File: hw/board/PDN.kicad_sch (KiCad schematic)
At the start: 47 parts, among them U1 XC7A35T-FTG256, U2 TPS54331DR, U3 AP7361C-18SP-13, U4 AP7361C-10E

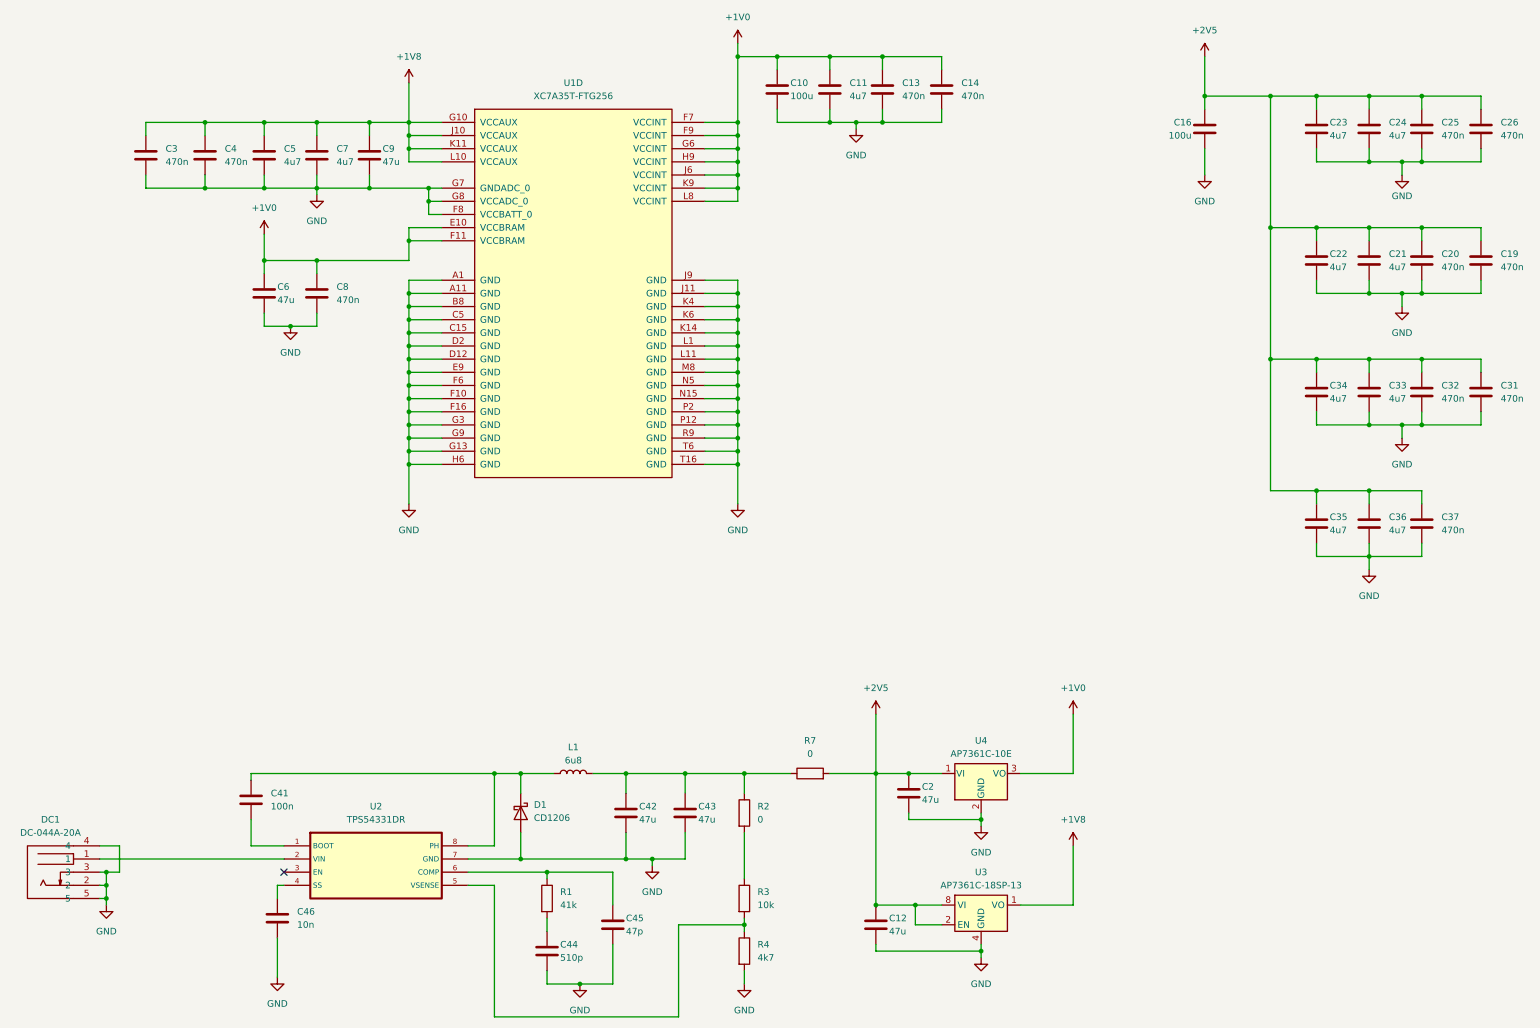
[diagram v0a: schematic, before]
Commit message: Reannotated piece numbers
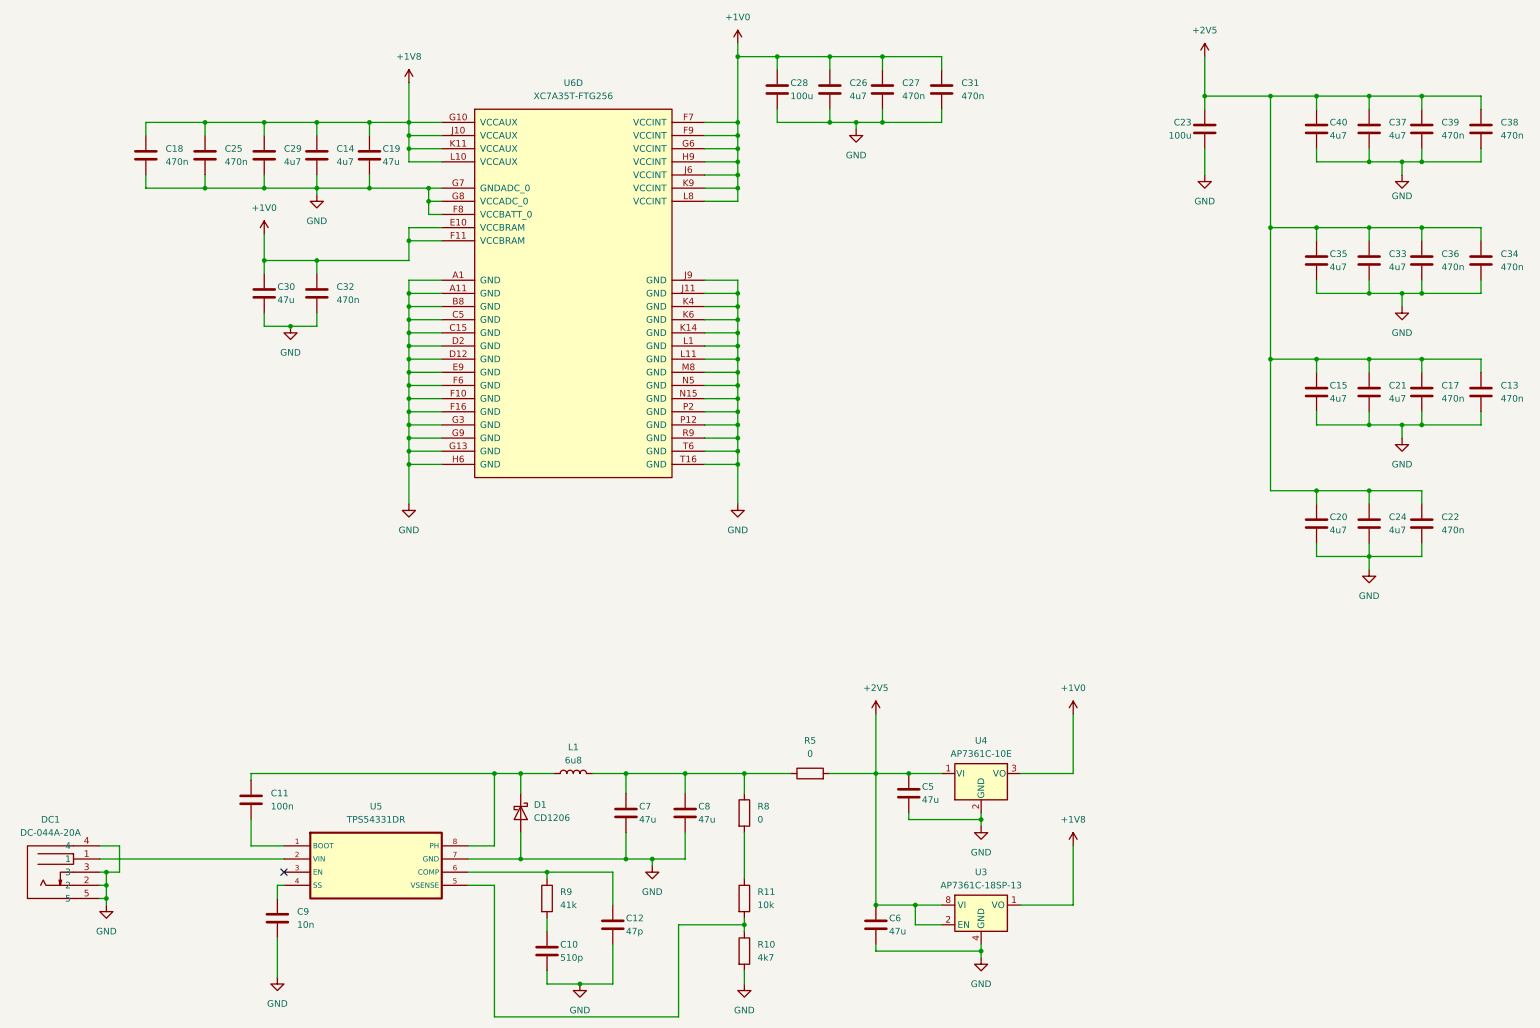
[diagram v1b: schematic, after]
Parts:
- renumbered C44 to C10, C41 to C11, C45 to C12, C31 to C13, C7 to C14, C34 to C15, C32 to C17, C3 to C18, C9 to C19, C35 to C20, C33 to C21, C37 to C22, C16 to C23, C36 to C24, C4 to C25, C11 to C26, C13 to C27, C10 to C28, C5 to C29, C6 to C30, C14 to C31, C8 to C32, C21 to C33, C19 to C34, C22 to C35, C20 to C36, C24 to C37, C26 to C38, C25 to C39, C23 to C40, C2 to C5, C12 to C6, C42 to C7, C43 to C8, C46 to C9, R4 to R10, R3 to R11, R7 to R5, R2 to R8, R1 to R9, U2 to U5, U1 to U6

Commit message: Added capacitor for STM32 NRST
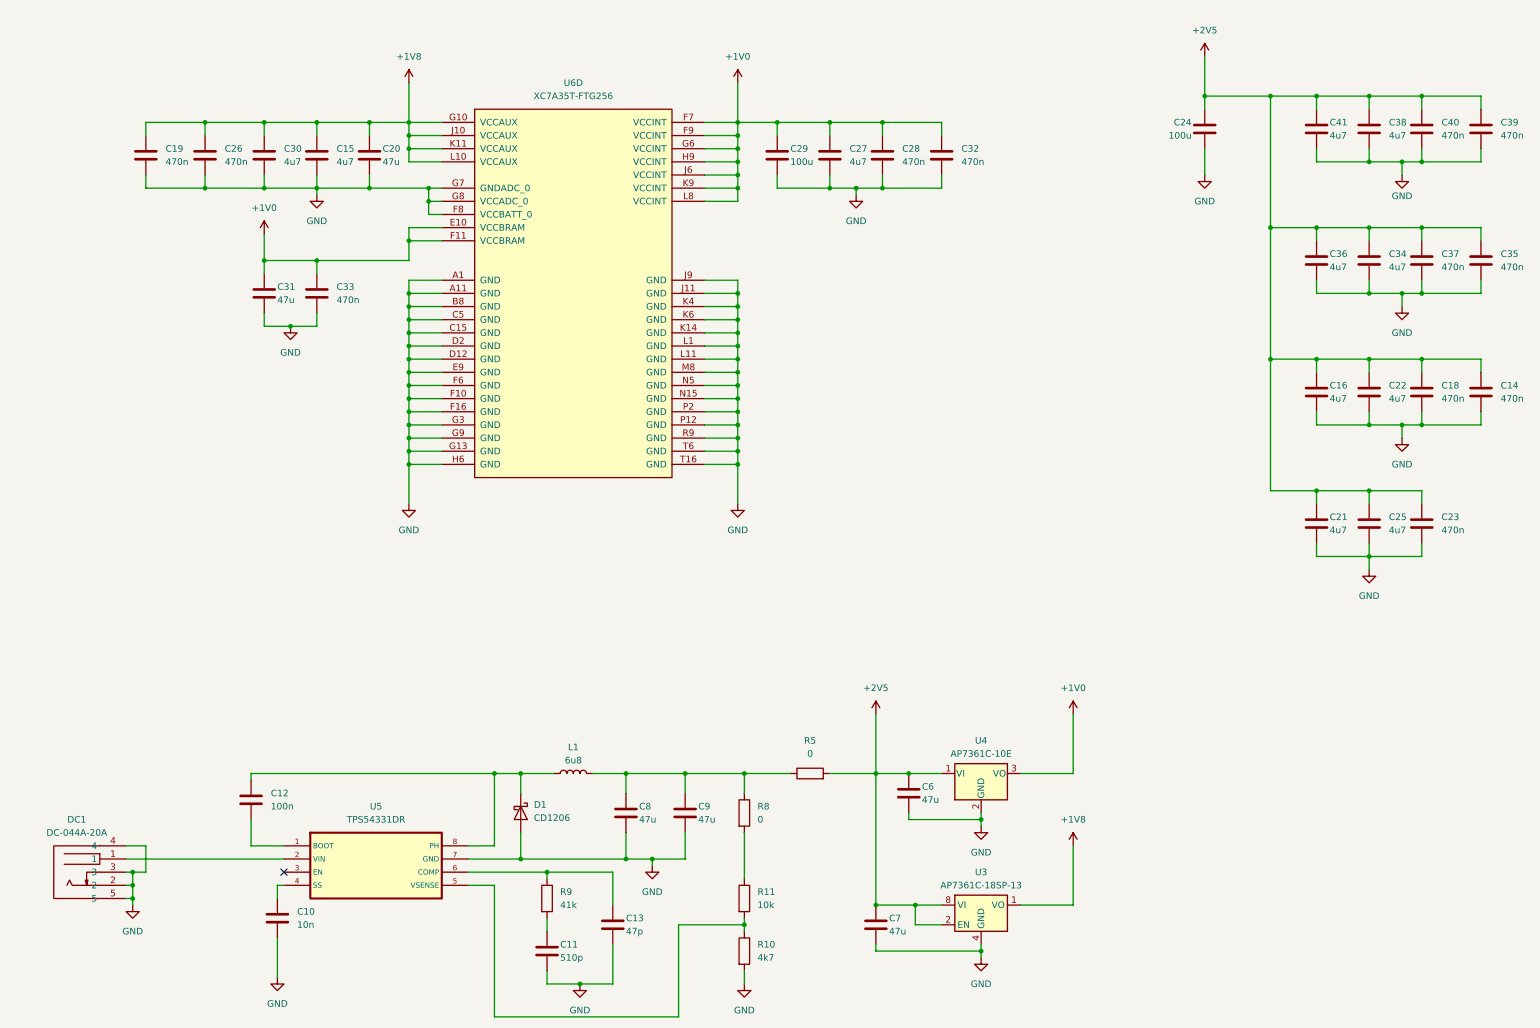
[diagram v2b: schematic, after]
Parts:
- renumbered C9 to C10, C10 to C11, C11 to C12, C12 to C13, C13 to C14, C14 to C15, C15 to C16, C17 to C18, C18 to C19, C19 to C20, C20 to C21, C21 to C22, C22 to C23, C23 to C24, C24 to C25, C25 to C26, C26 to C27, C27 to C28, C28 to C29, C29 to C30, C30 to C31, C31 to C32, C32 to C33, C33 to C34, C34 to C35, C35 to C36, C36 to C37, C37 to C38, C38 to C39, C39 to C40, C40 to C41, C5 to C6, C6 to C7, C7 to C8, C8 to C9
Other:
- moved on the sheet: C27, C28, C29, C32, DC1

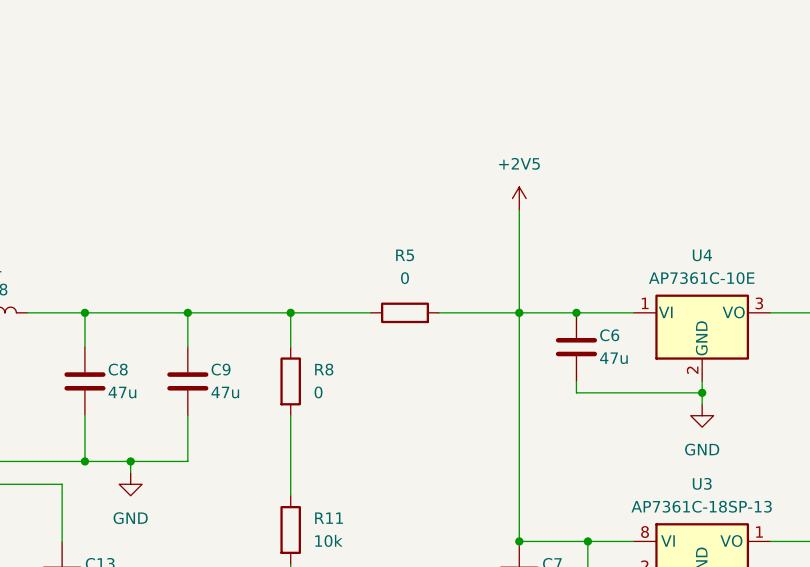
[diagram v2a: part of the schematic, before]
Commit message: Replaced inductor footprint
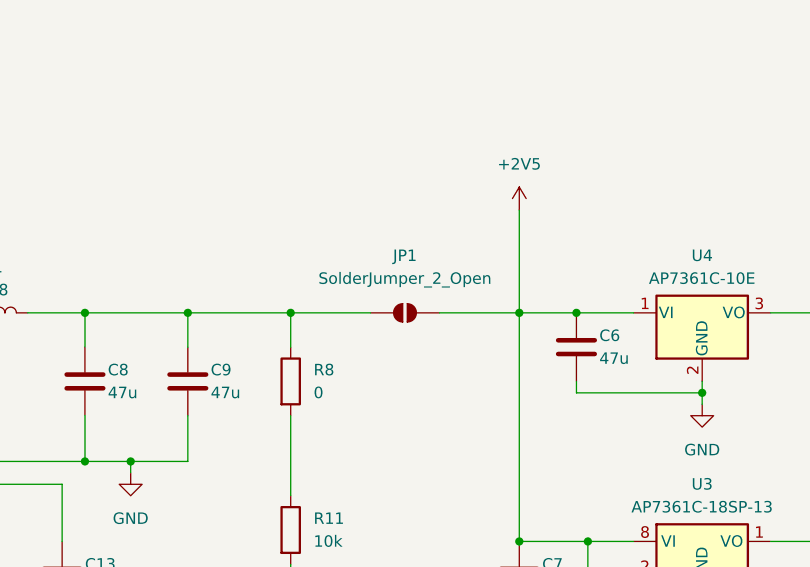
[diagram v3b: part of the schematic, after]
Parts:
- removed R5: 0, Resistor_SMD:R_1210_3225Metric, symbol Device:R
- added JP1: SolderJumper_2_Open, Jumper:SolderJumper-2_P1.3mm_Open_TrianglePad1.0x1.5mm, symbol Jumper:SolderJumper_2_Open
- L1: footprint Inductor_SMD:L_Chilisin_BMRF00101040 -> EasyEDA:IND-SMD_L11.6-W10.1
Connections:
- net +2V5: now also JP1.2 (B)
- net at C8.1, C9.1, L1.2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: now also JP1.1 (A)
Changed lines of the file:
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@@
 			)
 		)
-		(property "Footprint" "Inductor_SMD:L_Chilisin_BMRF00101040"
+		(property "Footprint" "EasyEDA:IND-SMD_L11.6-W10.1"
 			(at 119.38 163.83 0)
 			(effects
@@
 	)
 	(symbol
+		(lib_id "Jumper:SolderJumper_2_Open")
+		(at 165.1 163.83 0)
+		(unit 1)
+		(exclude_from_sim yes)
+		(in_bom no)
+		(on_board yes)
+		(dnp no)
+		(fields_autoplaced yes)
+		(property "Reference" "JP1"
+			(at 165.1 157.48 0)
+			(effects
+				(font
+					(size 1.27 1.27)
+				)
+			)
+		)
+		(property "Value" "SolderJumper_2_Open"
+			(at 165.1 160.02 0)
+			(effects
+				(font
+					(size 1.27 1.27)
+				)
+			)
+		)
+		(property "Footprint" "Jumper:SolderJumper-2_P1.3mm_Open_TrianglePad1.0x1.5mm"
+			(at 165.1 163.83 0)
+			(effects
+				(font
+					(size 1.27 1.27)
+				)
+				(hide yes)
+			)
+		)
+		(property "Datasheet" "~"
+			(at 165.1 163.83 0)
+			(effects
+				(font
+					(size 1.27 1.27)
+				)
+				(hide yes)
+			)
+		)
+		(property "Description" "Solder Jumper, 2-pole, open"
+			(at 165.1 163.83 0)
+			(effects
+				(font
+					(size 1.27 1.27)
+				)
+				(hide yes)
+			)
+		)
+		(pin "2"
+		)
+		(pin "1"
+		)
+		(instances
+			(project ""
+				(path "/0e384709-6bce-4dbf-a0e0-550e970390f4/eee0c0a3-ca6b-4ebc-bfd1-64a715a02fe6"
+					(reference "JP1")
+					(unit 1)
+				)
+			)
+		)
+	)
+	(symbol
 		(lib_id "power:GND")
 		(at 241.3 48.26 0)
@@
 					(unit 1)
 				)
-			)
-		)
-	)
-	(symbol
-		(lib_id "Device:R")
-		(at 165.1 163.83 90)
-		(unit 1)
-		(exclude_from_sim no)
-		(in_bom yes)
-		(on_board yes)
-		(dnp no)
-		(fields_autoplaced yes)
-		(property "Reference" "R5"
-			(at 165.1 157.48 90)
-			(effects
-				(font
-					(size 1.27 1.27)
-				)
-			)
-		)
-		(property "Value" "0"
-			(at 165.1 160.02 90)
-			(effects
-				(font
-					(size 1.27 1.27)
-				)
-			)
-		)
-		(property "Footprint" "Resistor_SMD:R_1210_3225Metric"
-			(at 165.1 165.608 90)
-			(effects
-				(font
-					(size 1.27 1.27)
-				)
-				(hide yes)
-			)
-		)
-		(property "Datasheet" "~"
-			(at 165.1 163.83 0)
-			(effects
-				(font
-					(size 1.27 1.27)
-				)
-				(hide yes)
-			)
-		)
-		(property "Description" "Resistor"
-			(at 165.1 163.83 0)
-			(effects
-				(font
-					(size 1.27 1.27)
-				)
-				(hide yes)
-			)
-		)
-		(pin "1"
-		)
-		(pin "2"
-		)
-		(instances
-			(project "board"
-				(path "/0e384709-6bce-4dbf-a0e0-550e970390f4/eee0c0a3-ca6b-4ebc-bfd1-64a715a02fe6"
-					(reference "R5")
-					(unit 1)
-				)

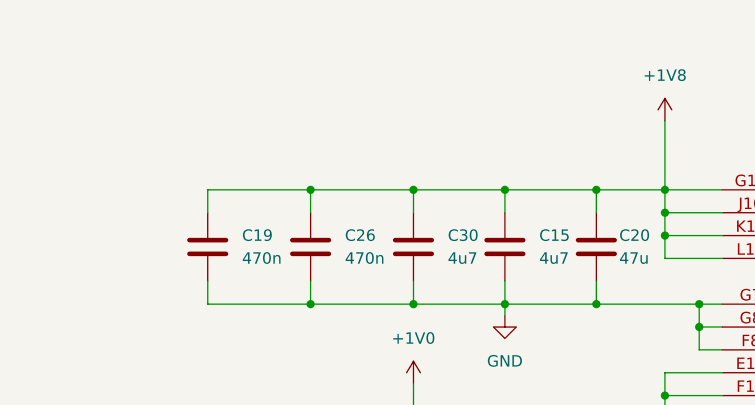
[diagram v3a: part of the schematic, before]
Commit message: Additional ground stitching vias
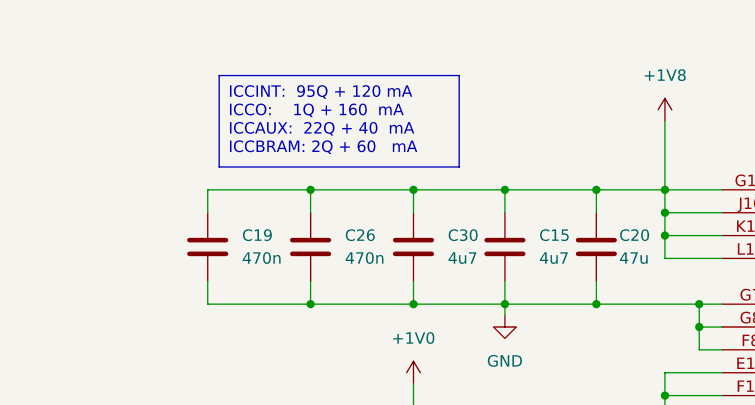
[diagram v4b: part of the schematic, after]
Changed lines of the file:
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@@
+		)
+	)
+	(text_box "ICCINT:  95Q + 120 mA\nICCO:    1Q + 160  mA\nICCAUX:  22Q + 40  mA\nICCBRAM: 2Q + 60   mA"
+		(exclude_from_sim no)
+		(at 38.1 25.4 0)
+		(size 26.67 10.16)
+		(stroke
+			(width 0)
+			(type default)
+		)
+		(fill
+			(type none)
+		)
+		(effects
+			(font
+				(size 1.27 1.27)
+			)
+			(justify left top)
 		)
 	)
